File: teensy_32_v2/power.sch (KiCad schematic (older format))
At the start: 38 parts, among them J1 277-1667-ND, J10 0878980426, J2 277-1667-ND, Q1 STL60P4LLF6, U2 MF-DSC-SOT233-BSS138, U3 RT7257G

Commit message: prep for order
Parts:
- J10: footprint Pin_Headers:Pin_Header_Straight_1x04_Pitch2.54mm_SMD_Pin1Right -> MF_Connectors:MF_Connectors-PTH_2.54MM_01X04
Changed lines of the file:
@@
 F 0 "J10" H 2400 4100 50  0000 C CNN
 F 1 "0878980426" H 2400 3600 50  0000 C CNN
-F 2 "Pin_Headers:Pin_Header_Straight_1x04_Pitch2.54mm_SMD_Pin1Right" H 2400 3900 50  0001 C CNN
+F 2 "MF_Connectors:MF_Connectors-PTH_2.54MM_01X04" H 2400 3900 50  0001 C CNN
 F 3 "" H 2400 3900 50  0001 C CNN
 	1    2400 3900

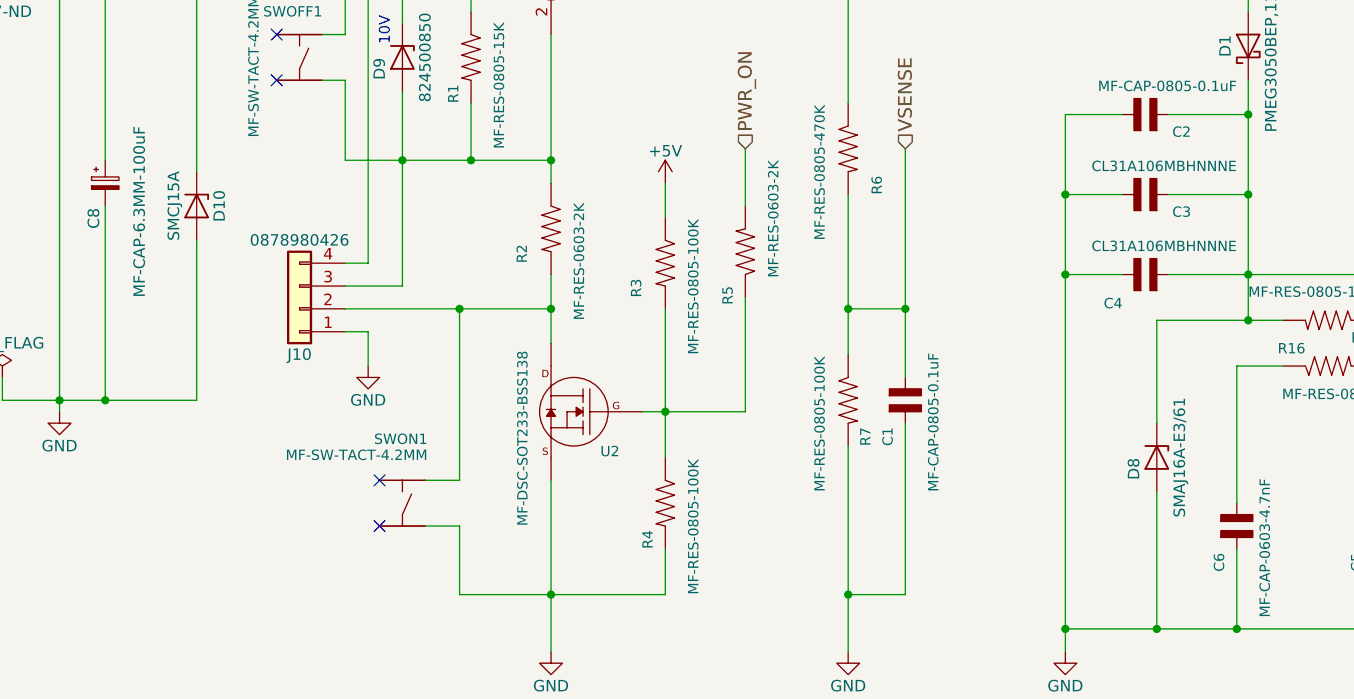
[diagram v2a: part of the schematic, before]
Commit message: tweaks to TVS diodes and board outline slot
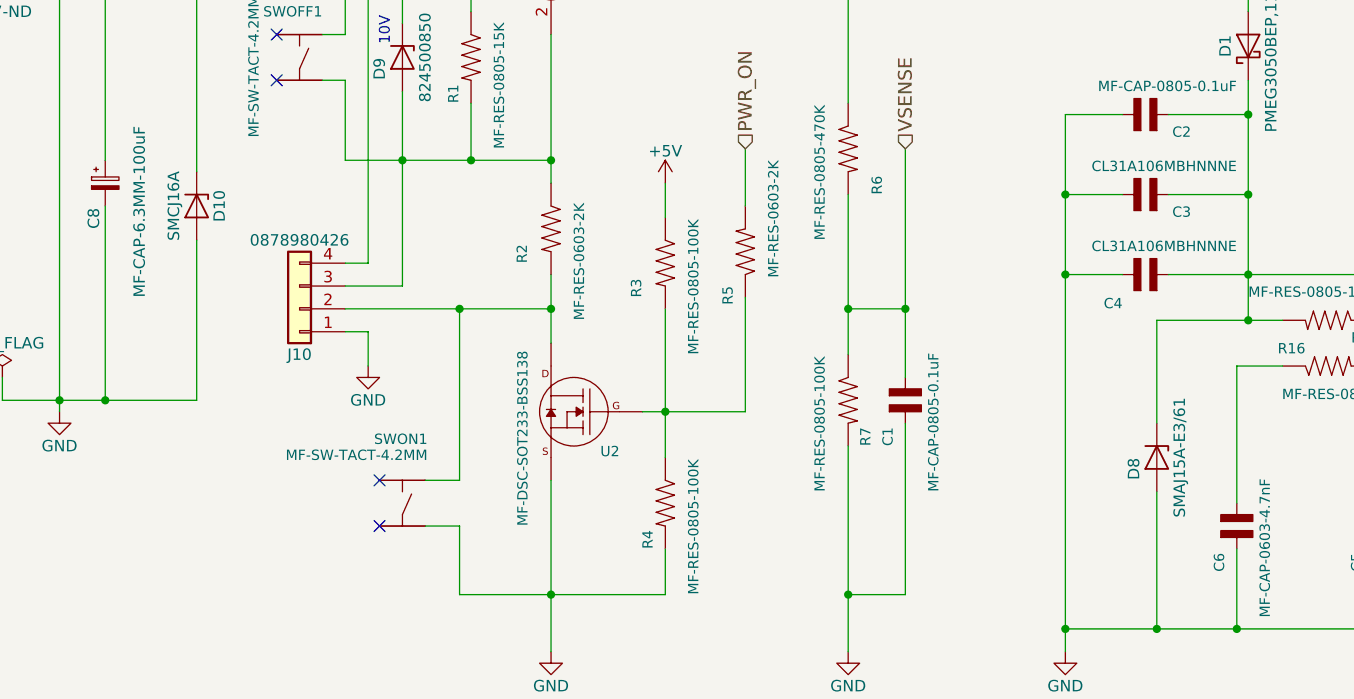
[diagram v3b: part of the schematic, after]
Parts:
- D10: value SMCJ15A -> SMCJ16A
- D8: value SMAJ16A-E3/61 -> SMAJ15A-E3/61
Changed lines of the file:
@@
 AR Path="/59ED6513/5A4B06E7" Ref="D8"  Part="1"
 F 0 "D8" H 6200 4450 50  0000 C CNN
-F 1 "SMAJ16A-E3/61" H 6150 4650 50  0000 C CNN
+F 1 "SMAJ15A-E3/61" H 6150 4650 50  0000 C CNN
 F 2 "Diodes_SMD:D_SMA_Standard" H 6150 4550 50  0001 C CNN
 F 3 "" H 6150 4550 50  0001 C CNN
@@
 P 1950 3450
 F 0 "D10" H 1950 3550 50  0000 C CNN
-F 1 "SMCJ15A" H 1950 3350 50  0000 C CNN
+F 1 "SMCJ16A" H 1950 3350 50  0000 C CNN
 F 2 "Diodes_SMD:D_SMC_Standard" H 1950 3450 50  0001 C CNN
 F 3 "" H 1950 3450 50  0001 C CNN
